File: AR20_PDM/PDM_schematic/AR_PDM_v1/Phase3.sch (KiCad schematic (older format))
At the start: 12 parts, among them Q3 BTS50025-1TAD, U6 INA233

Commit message: Alpha version DONE! - Gerber files generated
- Tweeked
- checked and re cheked
- added all missing components
- Created a really nice silkscreen
- Ready To Test
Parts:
- renumbered C_in1 to C12, C_out1 to C13, C_vs1 to C14, Cs1 to C15, C_bypass4 to C16, Q3 to Q2, R_in1 to R10, 4k7 to R11, R_s1 to R12, R_Shunt5 to R13, R7 to R9, U6 to U3

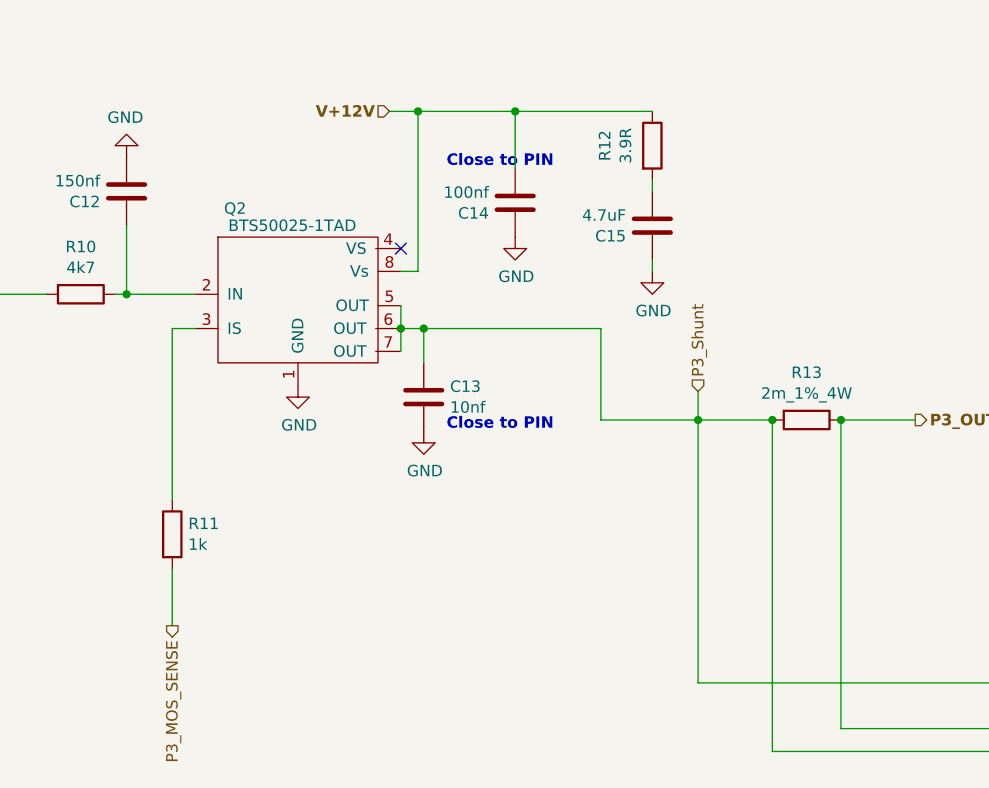
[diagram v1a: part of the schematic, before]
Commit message: Fixed wrong resistors, mos sense. Gerber files updated
- removed all R_is_protection resistors on each mosfet line
- added one R_is_protection resistors to mos_sense_all
ps, mux N-fets, does not need overvoltage protection. 60 volt tolerant.
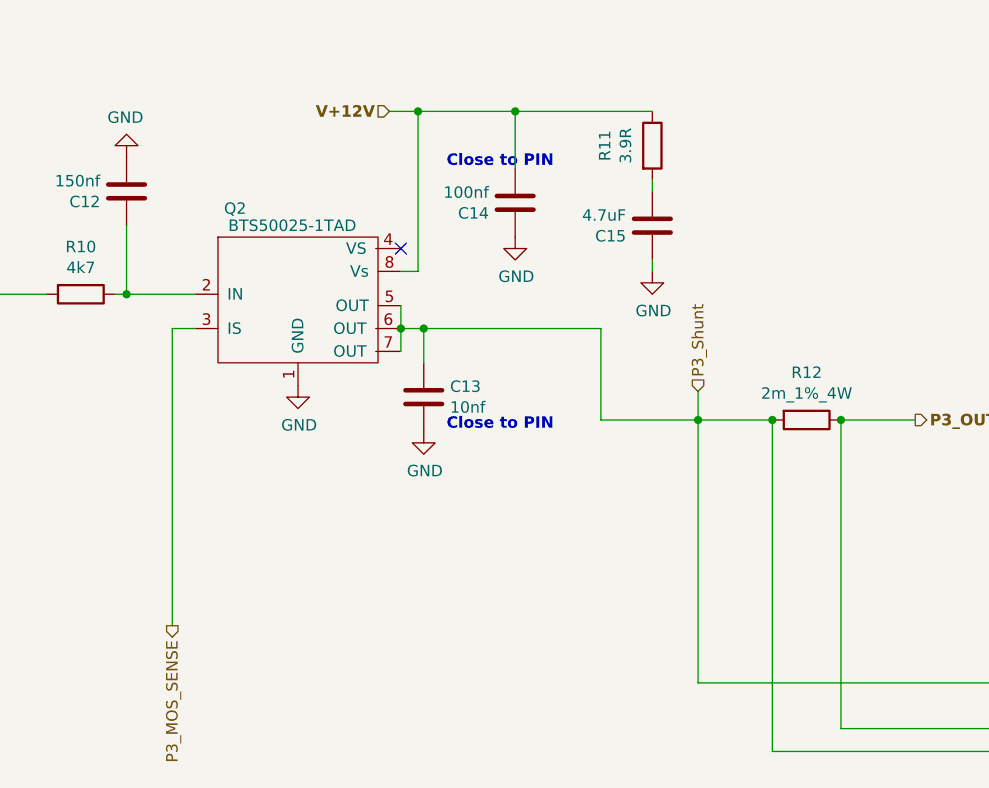
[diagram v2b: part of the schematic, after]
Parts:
- removed R11: 1k, Resistor_SMD:R_0603_1608Metric, symbol AR20_PDM_v1-rescue:R-Device
- renumbered R12 to R11, R13 to R12
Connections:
- net P3_MOS_SENSE: now also Q2.3 (IS)
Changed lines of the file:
@@
 	3700 2550 3800 2550
-Wire Wire Line
-	3700 3850 3700 3600
 Wire Wire Line
 	8750 2850 8750 3350
@@
 AR Path="/5E0E607C/5E21B86E" Ref="R?"  Part="1"
 AR Path="/5E0FB5C8/5E21B86E" Ref="R?"  Part="1"
-AR Path="/5E0FBBBD/5E21B86E" Ref="R12"  Part="1"
+AR Path="/5E0FBBBD/5E21B86E" Ref="R11"  Part="1"
 AR Path="/5E0FC3A2/5E21B86E" Ref="R?"  Part="1"
 AR Path="/5E0FCFDC/5E21B86E" Ref="R?"  Part="1"
 AR Path="/5E0FDCCC/5E21B86E" Ref="R?"  Part="1"
 AR Path="/5E10174B/5E21B86E" Ref="R?"  Part="1"
-F 0 "R12" V 5593 1750 50  0000 C CNN
+F 0 "R11" V 5593 1750 50  0000 C CNN
 F 1 "3.9R" V 5684 1750 50  0000 C CNN
 F 2 "Resistor_SMD:R_0603_1608Metric" V 5730 1750 50  0001 C CNN
@@
 Wire Wire Line
 	6000 4100 8750 4100
-$Comp
-L AR20_PDM_v1-rescue:R-Device R?
-U 1 1 5E21B876
-P 3700 3450
-AR Path="/5DA89415/5E21B876" Ref="R?"  Part="1"
-AR Path="/5DEB10A1/5E21B876" Ref="R?"  Part="1"
-AR Path="/5DEB20EA/5E21B876" Ref="R?"  Part="1"
-AR Path="/5E0E4725/5E21B876" Ref="R?"  Part="1"
-AR Path="/5E0E4A93/5E21B876" Ref="R?"  Part="1"
-AR Path="/5E0E4EB5/5E21B876" Ref="R?"  Part="1"
-AR Path="/5E0E5304/5E21B876" Ref="R?"  Part="1"
-AR Path="/5E0E594B/5E21B876" Ref="R?"  Part="1"
-AR Path="/5E0E607C/5E21B876" Ref="R?"  Part="1"
-AR Path="/5E0FB5C8/5E21B876" Ref="R?"  Part="1"
-AR Path="/5E0FBBBD/5E21B876" Ref="R11"  Part="1"
-AR Path="/5E0FC3A2/5E21B876" Ref="R?"  Part="1"
-AR Path="/5E0FCFDC/5E21B876" Ref="R?"  Part="1"
-AR Path="/5E0FDCCC/5E21B876" Ref="R?"  Part="1"
-AR Path="/5E10174B/5E21B876" Ref="R?"  Part="1"
-F 0 "R11" H 3770 3496 50  0000 L CNN
-F 1 "1k" H 3770 3405 50  0000 L CNN
-F 2 "Resistor_SMD:R_0603_1608Metric" V 3630 3450 50  0001 C CNN
-F 3 "~" H 3700 3450 50  0001 C CNN
-	1    3700 3450
-	1    0    0    -1
-$EndComp
 Wire Wire Line
 	6325 4400 8750 4400
@@
 AR Path="/5E0E607C/5E1CBF07" Ref="R?"  Part="1"
 AR Path="/5E0FB5C8/5E1CBF07" Ref="R?"  Part="1"
-AR Path="/5E0FBBBD/5E1CBF07" Ref="R13"  Part="1"
+AR Path="/5E0FBBBD/5E1CBF07" Ref="R12"  Part="1"
 AR Path="/5E0FC3A2/5E1CBF07" Ref="R?"  Part="1"
 AR Path="/5E0FCFDC/5E1CBF07" Ref="R?"  Part="1"
 AR Path="/5E0FDCCC/5E1CBF07" Ref="R?"  Part="1"
 AR Path="/5E10174B/5E1CBF07" Ref="R?"  Part="1"
-F 0 "R13" V 6268 2950 50  0000 C CNN
+F 0 "R12" V 6268 2950 50  0000 C CNN
 F 1 "2m_1%_4W" V 6359 2950 50  0000 C CNN
 F 2 "Resistor_SMD:R_2512_6332Metric" V 6405 2950 50  0001 C CNN
@@
 Connection ~ 6000 2950
 Wire Wire Line
-	3700 2550 3700 3300
-Wire Wire Line
 	4650 1600 4775 1600
 Wire Wire Line
@@
 Wire Wire Line
 	4775 1600 5200 1600
+Wire Wire Line
+	3700 2550 3700 3850
 $EndSCHEMATC

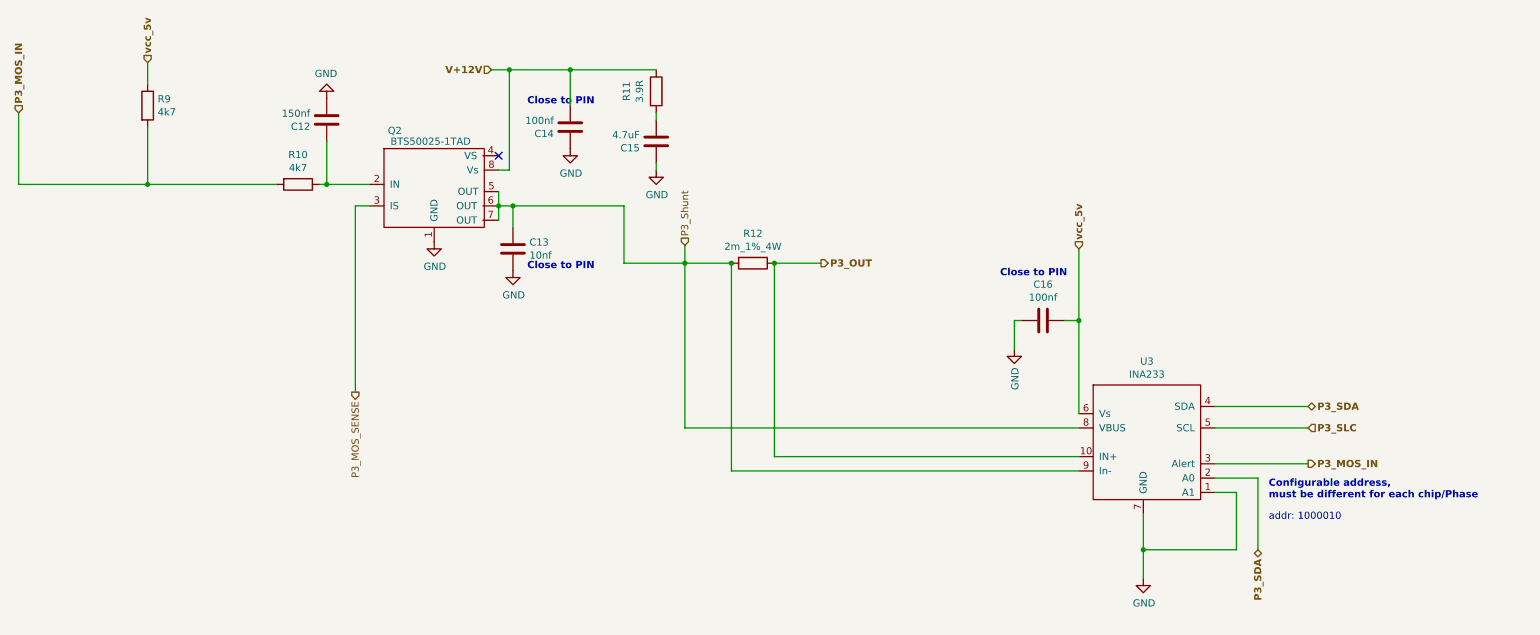
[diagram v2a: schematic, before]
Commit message: Major redesign. schematics completed, PCB work in progress
-TODO : A proper changelog file. Where all changes will apear 
- Redesigned schematics to accommodate errors in the improvement list
- More detail in ALPHA improvement list
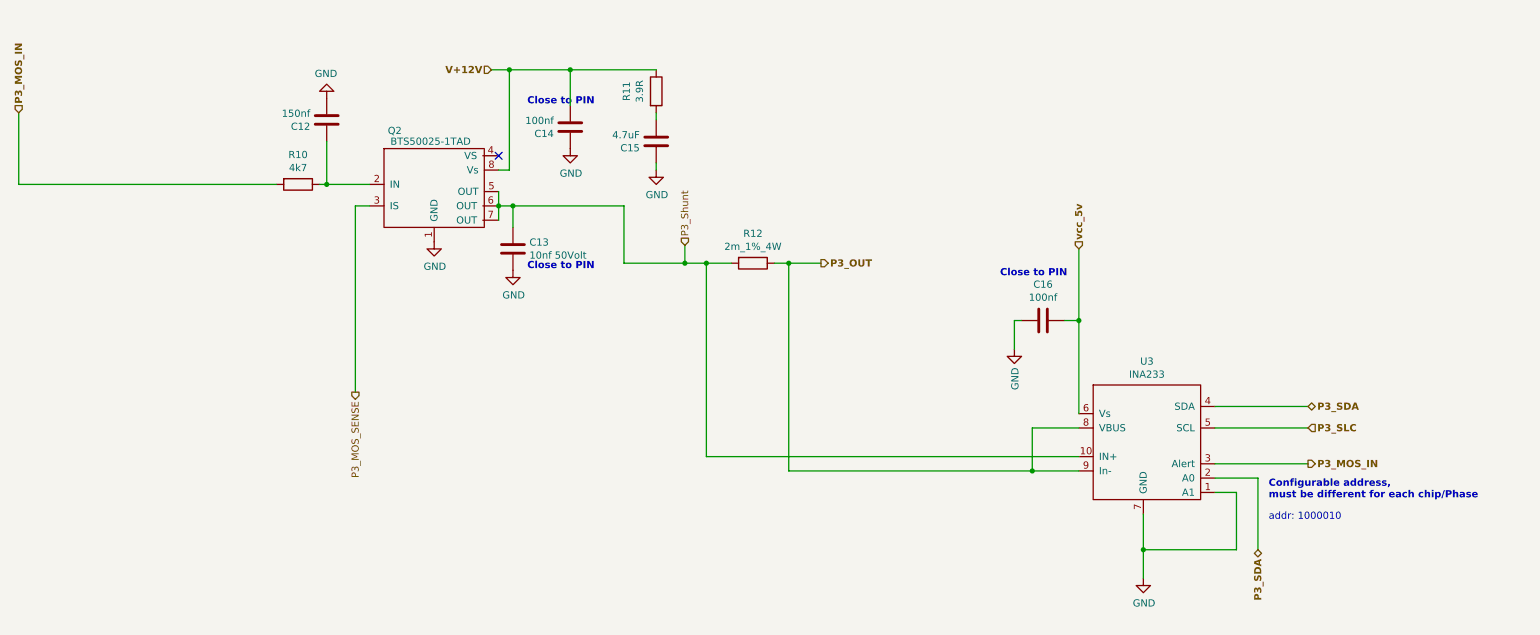
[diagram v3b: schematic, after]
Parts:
- removed R9: 4k7, Resistor_SMD:R_0603_1608Metric, symbol AR20_PDM_v1-rescue:R-Device
- C13: value 10nf -> 10nf 50Volt
- R11: footprint Resistor_SMD:R_0603_1608Metric -> Resistor_SMD:R_2512_6332Metric
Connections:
- net P3_OUT: now also U3.8 (VBUS), U3.9 (In-); no longer U3.10 (IN+)
- net P3_Shunt: now also U3.10 (IN+); no longer U3.8 (VBUS), U3.9 (In-)
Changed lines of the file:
@@
 $Descr A4 11693 8268
 encoding utf-8
-Sheet 3 13
+Sheet 3 14
 Title ""
 Date ""
@@
 AR Path="/5E10174B/5E21B80C" Ref="C?"  Part="1"
 F 0 "C13" H 4915 2896 50  0000 L CNN
-F 1 "10nf" H 4915 2805 50  0000 L CNN
+F 1 "10nf 50Volt" H 4915 2805 50  0000 L CNN
 F 2 "Capacitor_SMD:C_0603_1608Metric" H 4838 2700 50  0001 C CNN
 F 3 "~" H 4800 2850 50  0001 C CNN
@@
 $EndComp
 $Comp
-L AR20_PDM_v1-rescue:R-Device R?
-U 1 1 5E21B818
-P 2250 1850
-AR Path="/5DA89415/5E21B818" Ref="R?"  Part="1"
-AR Path="/5DEB10A1/5E21B818" Ref="R?"  Part="1"
-AR Path="/5DEB20EA/5E21B818" Ref="R?"  Part="1"
-AR Path="/5E0E4725/5E21B818" Ref="R?"  Part="1"
-AR Path="/5E0E4A93/5E21B818" Ref="R?"  Part="1"
-AR Path="/5E0E4EB5/5E21B818" Ref="R?"  Part="1"
-AR Path="/5E0E5304/5E21B818" Ref="R?"  Part="1"
-AR Path="/5E0E594B/5E21B818" Ref="R?"  Part="1"
-AR Path="/5E0E607C/5E21B818" Ref="R?"  Part="1"
-AR Path="/5E0FB5C8/5E21B818" Ref="R?"  Part="1"
-AR Path="/5E0FBBBD/5E21B818" Ref="R9"  Part="1"
-AR Path="/5E0FC3A2/5E21B818" Ref="R?"  Part="1"
-AR Path="/5E0FCFDC/5E21B818" Ref="R?"  Part="1"
-AR Path="/5E0FDCCC/5E21B818" Ref="R?"  Part="1"
-AR Path="/5E10174B/5E21B818" Ref="R?"  Part="1"
-F 0 "R9" H 2320 1896 50  0000 L CNN
-F 1 "4k7" H 2320 1805 50  0000 L CNN
-F 2 "Resistor_SMD:R_0603_1608Metric" V 2180 1850 50  0001 C CNN
-F 3 "~" H 2250 1850 50  0001 C CNN
-	1    2250 1850
-	1    0    0    -1
-$EndComp
-$Comp
 L AR20_PDM_v1-rescue:C-Device C?
 U 1 1 5E21B829
@@
 Text Notes 8200 3050 0    50   ~ 10
 Close to PIN
-Text HLabel 2250 1550 1    50   Input ~ 10
-vcc_5v
 Wire Wire Line
 	9700 4100 10350 4100
-Wire Wire Line
-	2250 1550 2250 1700
 $Comp
 L AR20_PDM_v1-rescue:C-Device C?
@@
 F 0 "R11" V 5593 1750 50  0000 C CNN
 F 1 "3.9R" V 5684 1750 50  0000 C CNN
-F 2 "Resistor_SMD:R_0603_1608Metric" V 5730 1750 50  0001 C CNN
+F 2 "Resistor_SMD:R_2512_6332Metric" V 5730 1750 50  0001 C CNN
 F 3 "~" H 5800 1750 50  0001 C CNN
 	1    5800 1750
@@
 Wire Wire Line
 	9700 4350 10350 4350
-Connection ~ 2250 2400
-Wire Wire Line
-	2250 2000 2250 2400
 Wire Wire Line
 	1350 1900 1350 2400
-Wire Wire Line
-	1350 2400 2250 2400
 Wire Wire Line
 	9200 4950 9200 5150
@@
 	5575 2550 5575 2950
 Connection ~ 4800 2550
-Wire Wire Line
-	6000 4100 8750 4100
-Wire Wire Line
-	6325 4400 8750 4400
-Wire Wire Line
-	6625 4300 8750 4300
 Text HLabel 3700 3850 3    50   Output ~ 0
 P3_MOS_SENSE
@@
 V+12V
 Wire Wire Line
-	2250 2400 3150 2400
-Wire Wire Line
-	6625 2950 6625 4300
-Wire Wire Line
-	6325 2950 6325 4400
-Wire Wire Line
-	6000 2950 6325 2950
+	6000 2950 6150 2950
 $Comp
 L AR20_PDM_v1-rescue:R-Device R?
@@
 $EndComp
 Wire Wire Line
-	6625 2950 6950 2950
-Connection ~ 6325 2950
-Connection ~ 6625 2950
+	6625 2950 6725 2950
 Text Notes 10075 4750 0    50   ~ 0
 addr: 1000010
@@
 	4700 2550 4700 2450
 Wire Wire Line
-	6000 4100 6000 2950
-Wire Wire Line
 	6000 2950 6000 2825
 Text HLabel 6000 2825 1    50   Input ~ 0
@@
 Wire Wire Line
 	3700 2550 3700 3850
+Wire Wire Line
+	1350 2400 3150 2400
+Wire Wire Line
+	8750 4300 6150 4300
+Wire Wire Line
+	6150 4300 6150 2950
+Wire Wire Line
+	8750 4400 8425 4400
+Wire Wire Line
+	6725 4400 6725 2950
+Wire Wire Line
+	8750 4100 8425 4100
+Wire Wire Line
+	8425 4100 8425 4400
+Connection ~ 8425 4400
+Wire Wire Line
+	8425 4400 6725 4400
+Connection ~ 6150 2950
+Wire Wire Line
+	6150 2950 6325 2950
+Connection ~ 6725 2950
+Wire Wire Line
+	6725 2950 6950 2950
 $EndSCHEMATC

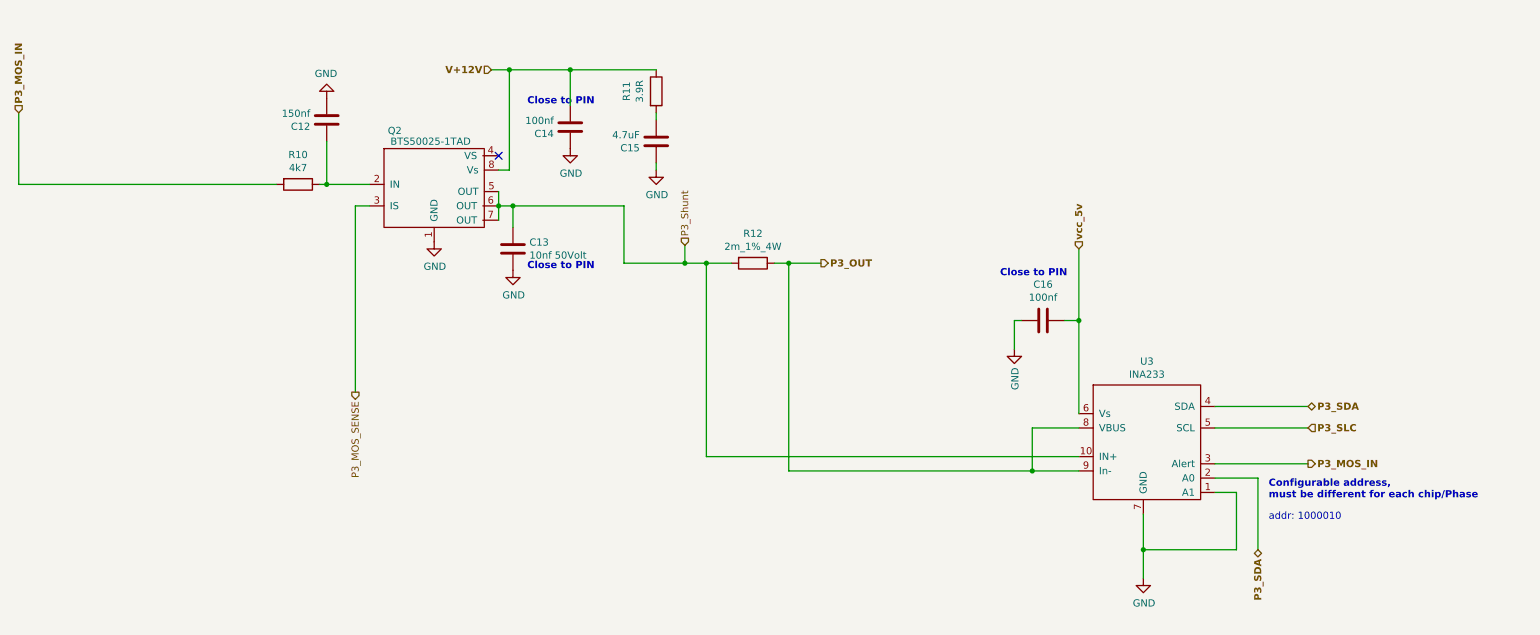
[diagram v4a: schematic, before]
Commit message: schematics rework
Fixed INA233 frying due to inductive flyback:
- Paced ina233 high side of the mosftets
- New input protection reseistors, and zener diodes, on each ina233.
Simplified:
- Removed the MUX and mos sense lines, as i realize that most of this functionality can be obtained trough INA233.
- Removed some of the cappacitors , besides the most needed ones.
- removed  back to back zener diode configuration, now a single diode insted.
 to reduce negative voltage in case of loss of VS, to be easy on the INA233 filters.
new stuff:
- Another temp sensor.
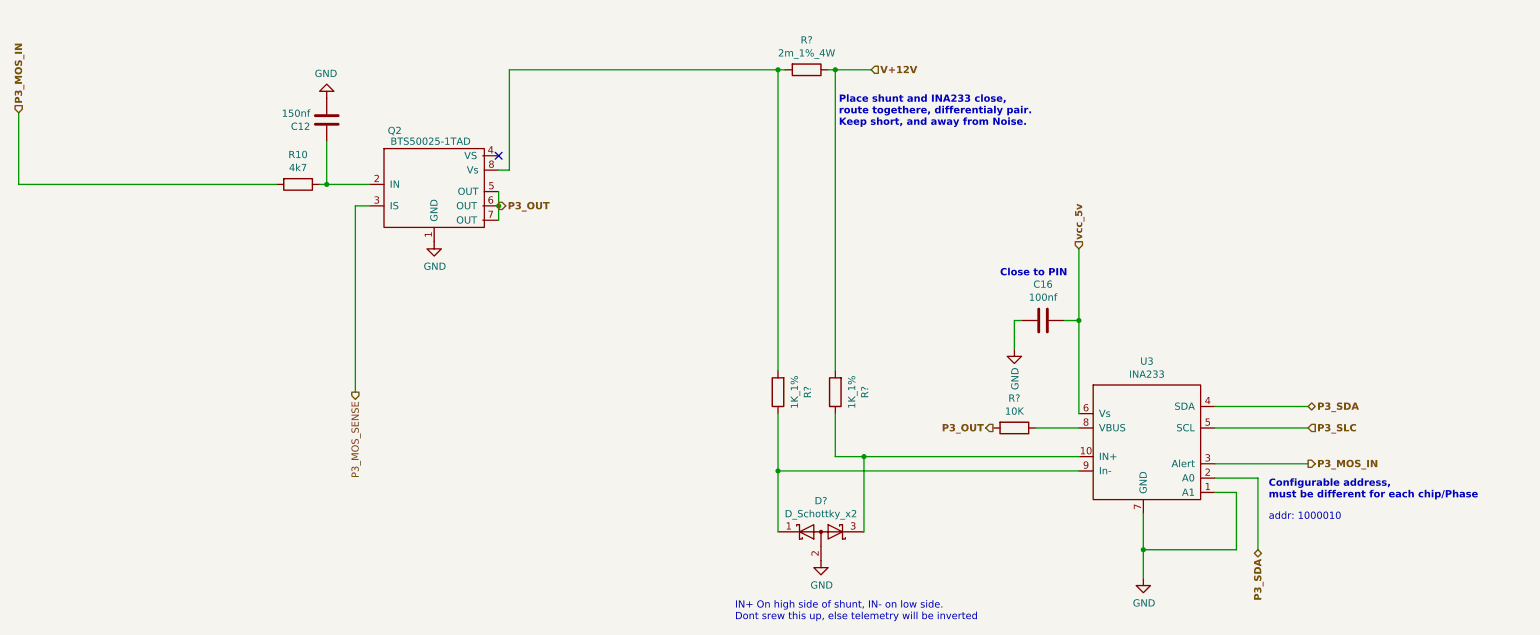
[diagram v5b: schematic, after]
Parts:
- removed C13: 10nf 50Volt, Capacitor_SMD:C_0603_1608Metric, symbol AR20_PDM_v1-rescue:C-Device
- removed C14: 100nf, Capacitor_SMD:C_0603_1608Metric, symbol AR20_PDM_v1-rescue:C-Device
- removed C15: 4.7uF, Capacitor_SMD:C_1206_3216Metric, symbol AR20_PDM_v1-rescue:C-Device
- removed R11: 3.9R, Resistor_SMD:R_2512_6332Metric, symbol AR20_PDM_v1-rescue:R-Device
- removed R12: 2m_1%_4W, Resistor_SMD:R_2512_6332Metric, symbol AR20_PDM_v1-rescue:R-Device
- added D?: D_Schottky_x2, symbol AR20_PDM_v1-rescue:D_Schottky_x2
- added R?: 2m_1%_4W, Resistor_SMD:R_2512_6332Metric, symbol AR20_PDM_v1-rescue:R-Device
- added R? (x2): 1K_1%, Resistor_SMD:R_0603_1608Metric, symbol AR20_PDM_v1-rescue:R-Device
- added R?: 10K, Resistor_SMD:R_0603_1608Metric, symbol AR20_PDM_v1-rescue:R-Device
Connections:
- net GND: now also D?.2 (A)
- net P3_OUT: now also Q2.5 (OUT), Q2.6 (OUT), Q2.7 (OUT), R?.2; no longer U3.8 (VBUS), U3.9 (In-)
- net V+12V: now also R?.1, R?.2; no longer Q2.8 (Vs)
- removed net P3_Shunt: Q2.5 (OUT), Q2.6 (OUT), Q2.7 (OUT), U3.10 (IN+)
- new net: D?.3 (K), R?.1, U3.10 (IN+)
- new net: R?.1, U3.8 (VBUS)
- new net: D?.1 (K), R?.1, U3.9 (In-)
- new net: Q2.8 (Vs), R?.2, R?.2
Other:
- note added: "IN+ On high side of shunt, IN- on low side.\nDont srew this up, else telemetry will be inverted"
- note added: "Place shunt and INA233 close, \nroute togethere, differentialy pair. \nKeep short, and away from Noise."
